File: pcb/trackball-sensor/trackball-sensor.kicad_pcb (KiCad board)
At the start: 2 copper layers, 22 x 48 mm, 16 parts, among them J1 Conn_01x01, J2 Conn_01x01, J3 Conn_01x01, J4 Conn_01x01, J5 Conn_01x01, J6 Conn_01x01, J7 Conn_01x01, Q1 Q_PMOS_GDS, U1 ADNS-9800

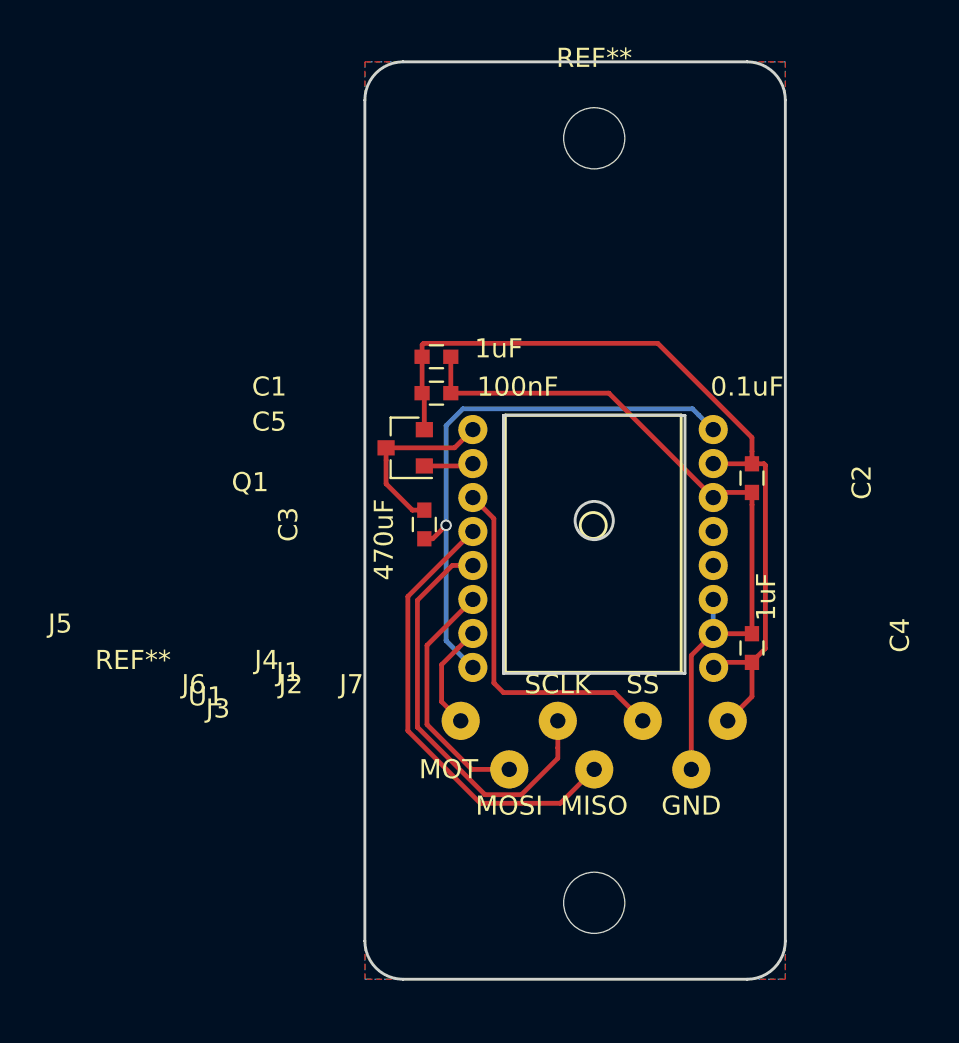
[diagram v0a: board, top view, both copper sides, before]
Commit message: sensor pcb: improve silk
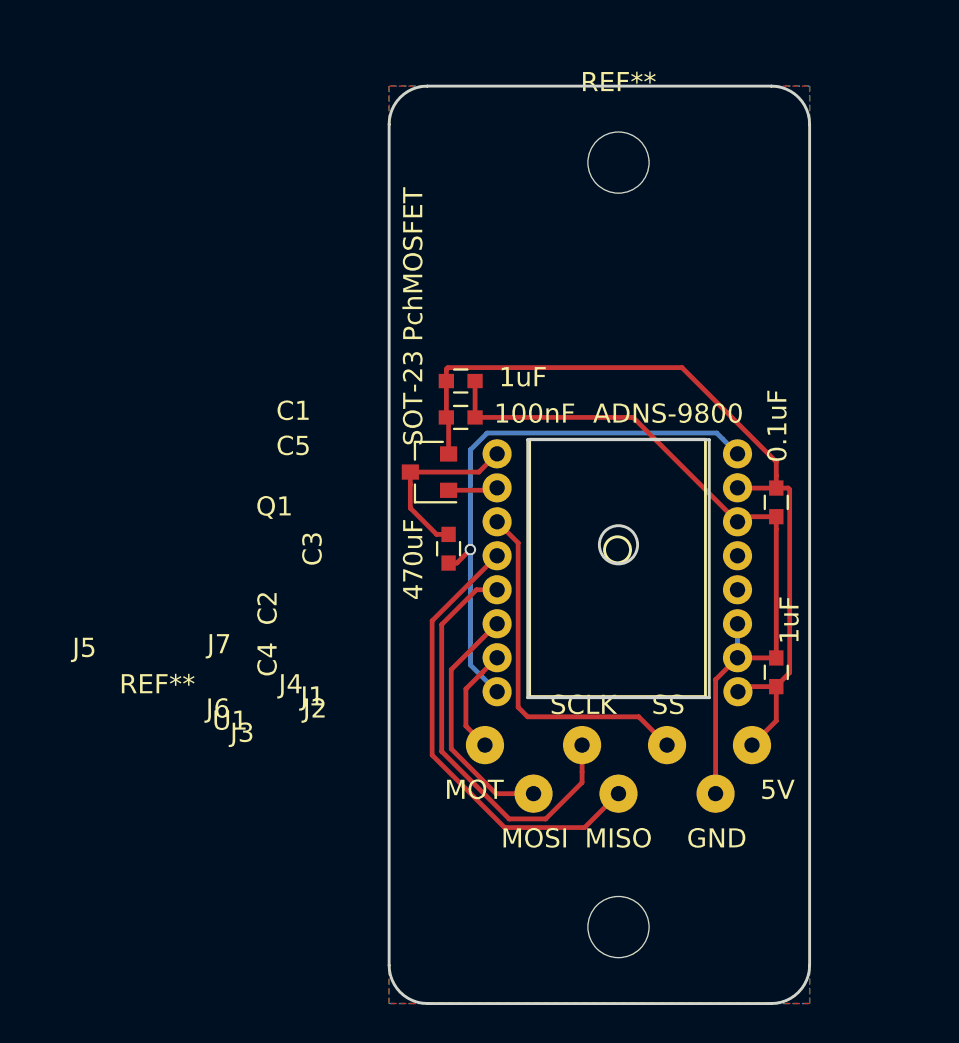
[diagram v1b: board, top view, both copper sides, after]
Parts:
- moved J5 1.80 mm to (15.8, 35.8)
- moved J6 1.80 mm to (6.29, 35.8)
- moved C3 1.80 mm to (4.38, 25.5)
- moved J1 1.80 mm to (20.3, 35.8)
- moved J2 1.80 mm to (11.4, 35.8)
- moved REF** 1.80 mm to (13.3, 45.3)
- moved U1 1.80 mm to (6.92, 20.5)
- moved Q1 1.80 mm to (3.38, 21.5)
- moved C1 1.80 mm to (5.01, 16.7)
- moved C2 1.80 mm to (21.5, 23.1)
- moved C4 1.80 mm to (21.5, 31.9)
- moved C5 1.80 mm to (5.01, 18.6)
- moved J7 1.80 mm to (18.4, 38.3)
- moved REF** 1.80 mm to (13.3, 5.27)
- moved J3 1.80 mm to (8.82, 38.3)
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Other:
- board text added: "5V"
- board text added: "ADNS-9800"
- board text added: "SOT-23 PchMOSFET"
